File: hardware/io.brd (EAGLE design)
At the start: 124 x 68 mm, 41 parts, among them IC1 LM2902D, IC2 LM2902D, U1 MMBT2222ALT1G, U2 MMBT2222ALT1G

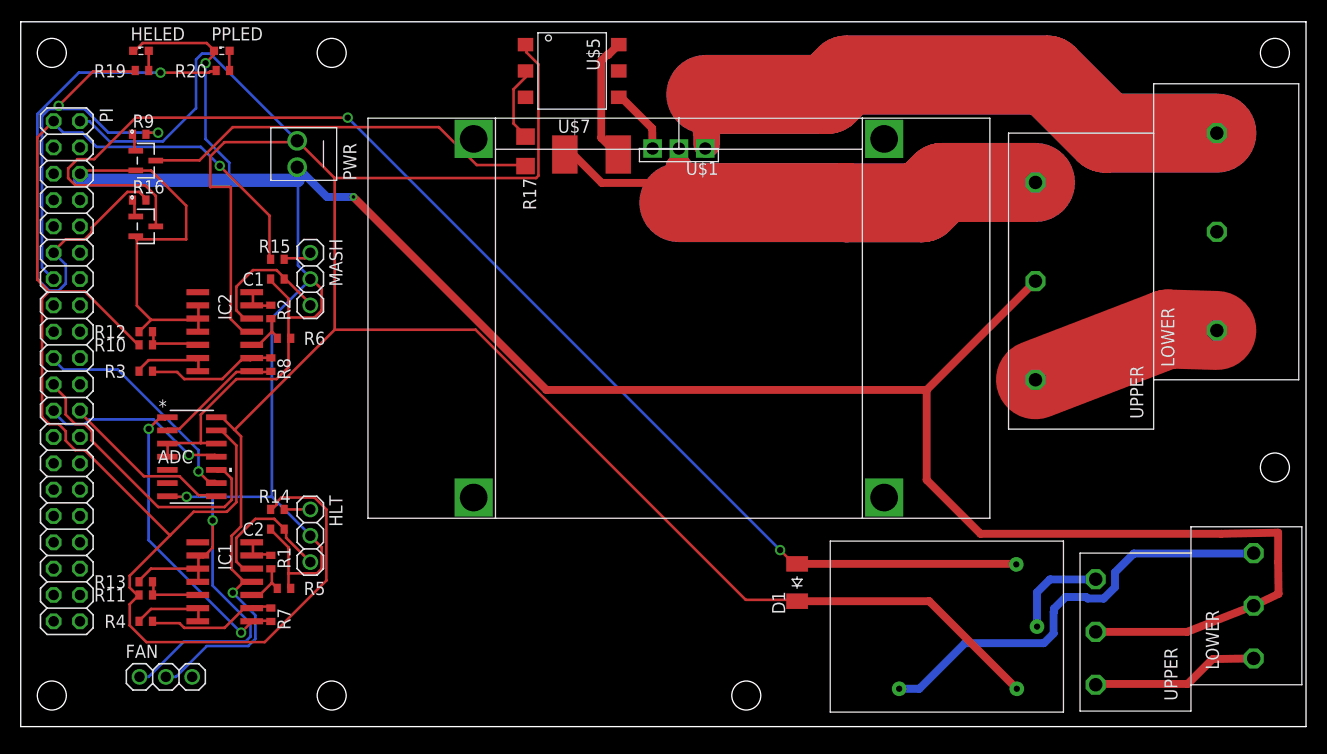
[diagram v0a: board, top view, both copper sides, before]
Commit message: IO and Relay boards are distinct
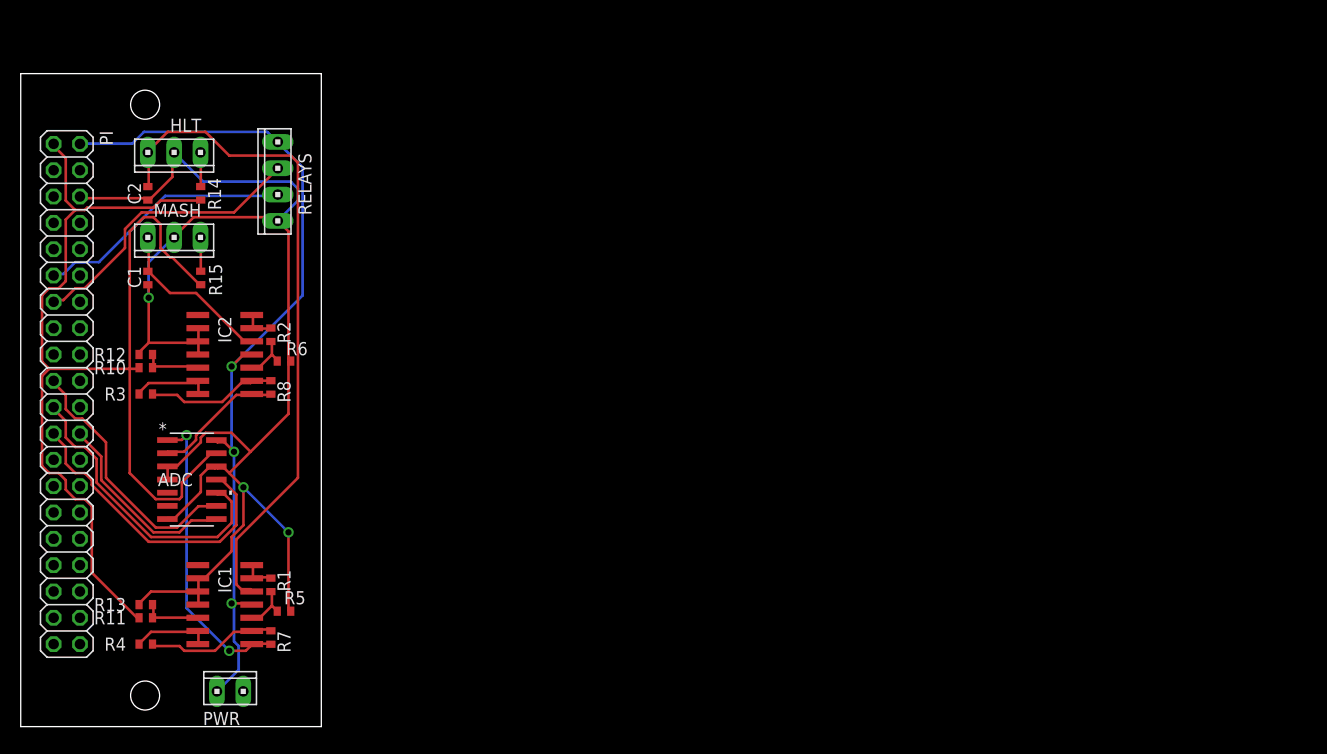
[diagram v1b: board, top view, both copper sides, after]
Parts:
- removed D1: CGRM4001-G, diode:SOD-123_MINI-SMA
- removed FAN: (no value), adafruit:1X03
- removed HELED, PPLED: (no value), eagle-ltspice:LED_SML0603
- removed R16, R9: 1K, resistor:R0402
- removed R17: 330, resistor:R1206
- removed R19, R20: 220, rcl:R0402
- removed U$1: T3050H-6I, digikey:TO-220
- removed U$2: VM1-038-1AEHORIZONTAL, digikey:VM2-038-1AE
- removed U$3: G5LE-1A4_DC5, digikey:G5LE-1A4_DC5
- removed U$4: PC1725041, digikey:PC-MKKDS1.5/3-5.08
- removed U$5: MOC3020S, digikey:6-SMD
- removed U$6: PC1719028, digikey:PC-MKKDS5/3-9.5
- removed U$7: CRM2512, digikey:2512(6432METRIC)
- removed U1, U2: MMBT2222ALT1G, digikey:SOT-23
- added RELAYS: (no value), con-amp:10X04MTA
- HLT, MASH: device adafruit:1X03 -> con-amp:10X03MTA
- PWR: value MTA-100-2HDR2 -> (none); device digikey:HDR2 -> con-amp:10X02MTA
- moved PWR 52.2 mm to (20.2, 3.40)
- moved HLT 39.2 mm to (14.8, 55.4), turned to 180 degrees
- moved C2 34.7 mm to (12.3, 51.5), turned to 270 degrees
- moved R14 31.4 mm to (17.4, 51.5), turned to 270 degrees
- moved MASH 13.7 mm to (14.8, 47.2), turned to 180 degrees
- moved C1 12.5 mm to (12.3, 43.3), turned to 270 degrees
- moved R15 7.62 mm to (17.4, 43.3), turned to 270 degrees
- moved IC2 2.20 mm to (19.7, 35.9)
- moved R12 2.20 mm to (12.1, 35.9)
- moved R2 2.20 mm to (24.1, 37.8)
- moved R6 2.20 mm to (25.4, 35.3)
- moved IC1 2.20 mm to (19.7, 11.8)
- moved R13 2.20 mm to (12.1, 11.8)
- moved R5 2.20 mm to (25.4, 11.1)
- moved R4 2.20 mm to (12.1, 7.96)
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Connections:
- removed net +120: U$6.P$1, U$6.P$4
- removed net -120: U$1.A1, U$6.P$3
- removed net 120H: U$3.P$1, U$4.P$3
- removed net 120N: U$4.P$1, U$4.P$4
- removed net N$13: R17.1, U1.3
- removed net N$14: R17.2, U$5.P$5
- removed net N$15: R9.1, U1.1
- removed net N$16: R16.1, U2.1
- removed net N$18: D1.A, U$3.P$2, U2.3
- removed net N$19: U$1.G, U$5.P$3
- removed net N$20: U$5.P$1, U$7.P$1
- removed net N$22: U$1.A2, U$6.P$6, U$7.P$2
- removed net N$24: U$3.P$3, U$4.P$6
- removed net N$25: HELED.A, R19.2
- removed net N$26: PPLED.A, R20.2
- net +5V: now also PWR.2, RELAYS.1; no longer D1.C, FAN.2, PWR.A1, U$3.P$4, U$5.P$6
- net GND: now also RELAYS.4; no longer FAN.1, HELED.C, PPLED.C, PWR.A2, U$4.P$2, U$4.P$5, U$6.P$5, U1.2, U2.2
- net HEOUT: now also RELAYS.2; no longer R19.1, R9.2
- net IN1: now also HLT.1; no longer HLT.3
- net IN2: now also MASH.1; no longer MASH.3
- net N$11: now also MASH.3; no longer MASH.1
- net N$12: now also HLT.3; no longer HLT.1
- net PPOUT: now also RELAYS.3; no longer R16.2, R20.1
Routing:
- net GND: track 375.6 -> 146.5 mm, vias 4 -> 3
- net +5V: track 243.9 -> 84.8 mm, vias 1 -> 3
- net N$18: track 124.4 -> 0.00 mm, vias 2 -> 0
- net -120: track 116.3 -> 0.00 mm
- net N$22: track 95.5 -> 0.00 mm
- net IN1: track 14.1 -> 64.9 mm
- net 120H: track 42.0 -> 0.00 mm
- net N$13: track 38.6 -> 0.00 mm
- net PPOUT: track 54.0 -> 24.9 mm, vias 1 -> 0
- net +3V3: track 149.6 -> 122.0 mm, vias 1 -> 0
- net +120: track 18.4 -> 0.00 mm
- net 120N: track 16.5 -> 0.00 mm
- net N$20: track 12.1 -> 0.00 mm
- net SPI_CLK: track 18.0 -> 29.4 mm, vias 1 -> 0
- net HEOUT: track 39.0 -> 28.1 mm, vias 2 -> 0
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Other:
- board size 124 x 68 mm -> 29 x 63 mm
